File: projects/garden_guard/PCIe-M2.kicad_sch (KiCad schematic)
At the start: 24 parts, among them J4 Bus_M.2_Socket_M, M1 M.2 Screw, M2 M.2 Solder Nut, M3 M.2 Solder Nut, M4 M.2 Solder Nut, M5 M.2 Solder Nut, U7 ASEK-32.768KHZ-L-R-T, U8 AP3441SHE-7B

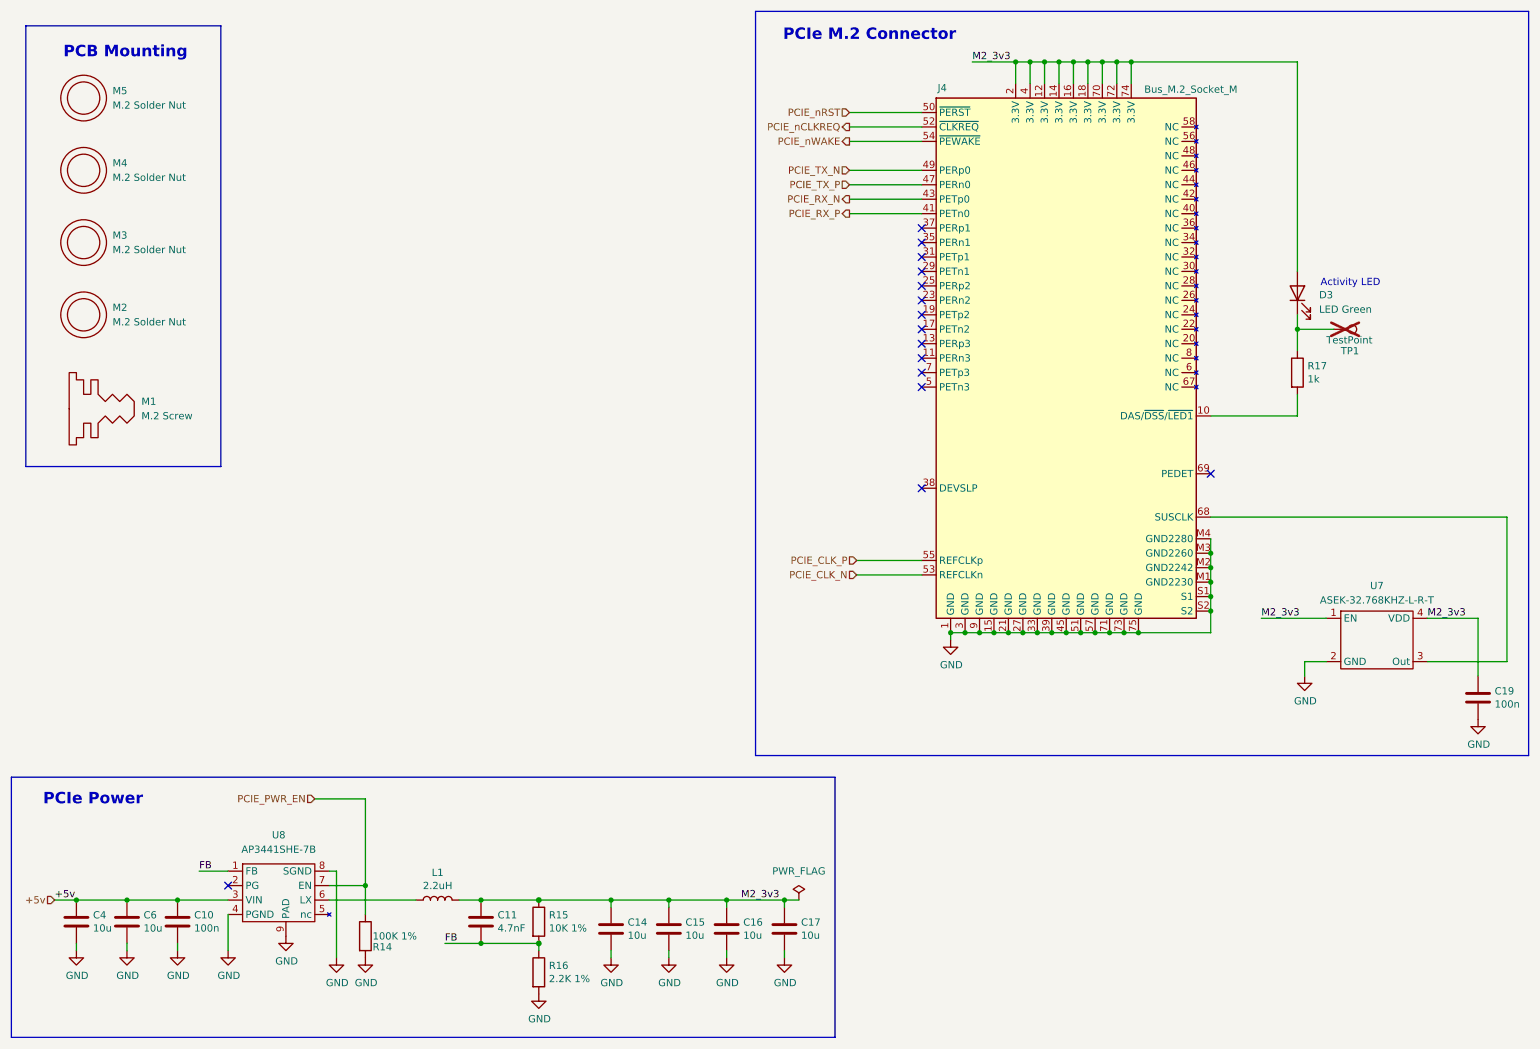
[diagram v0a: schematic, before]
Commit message: - Add PoE 12V power module - Add 12V->5V buck - Add automatic power source selection between PoE 5V and USB 5V
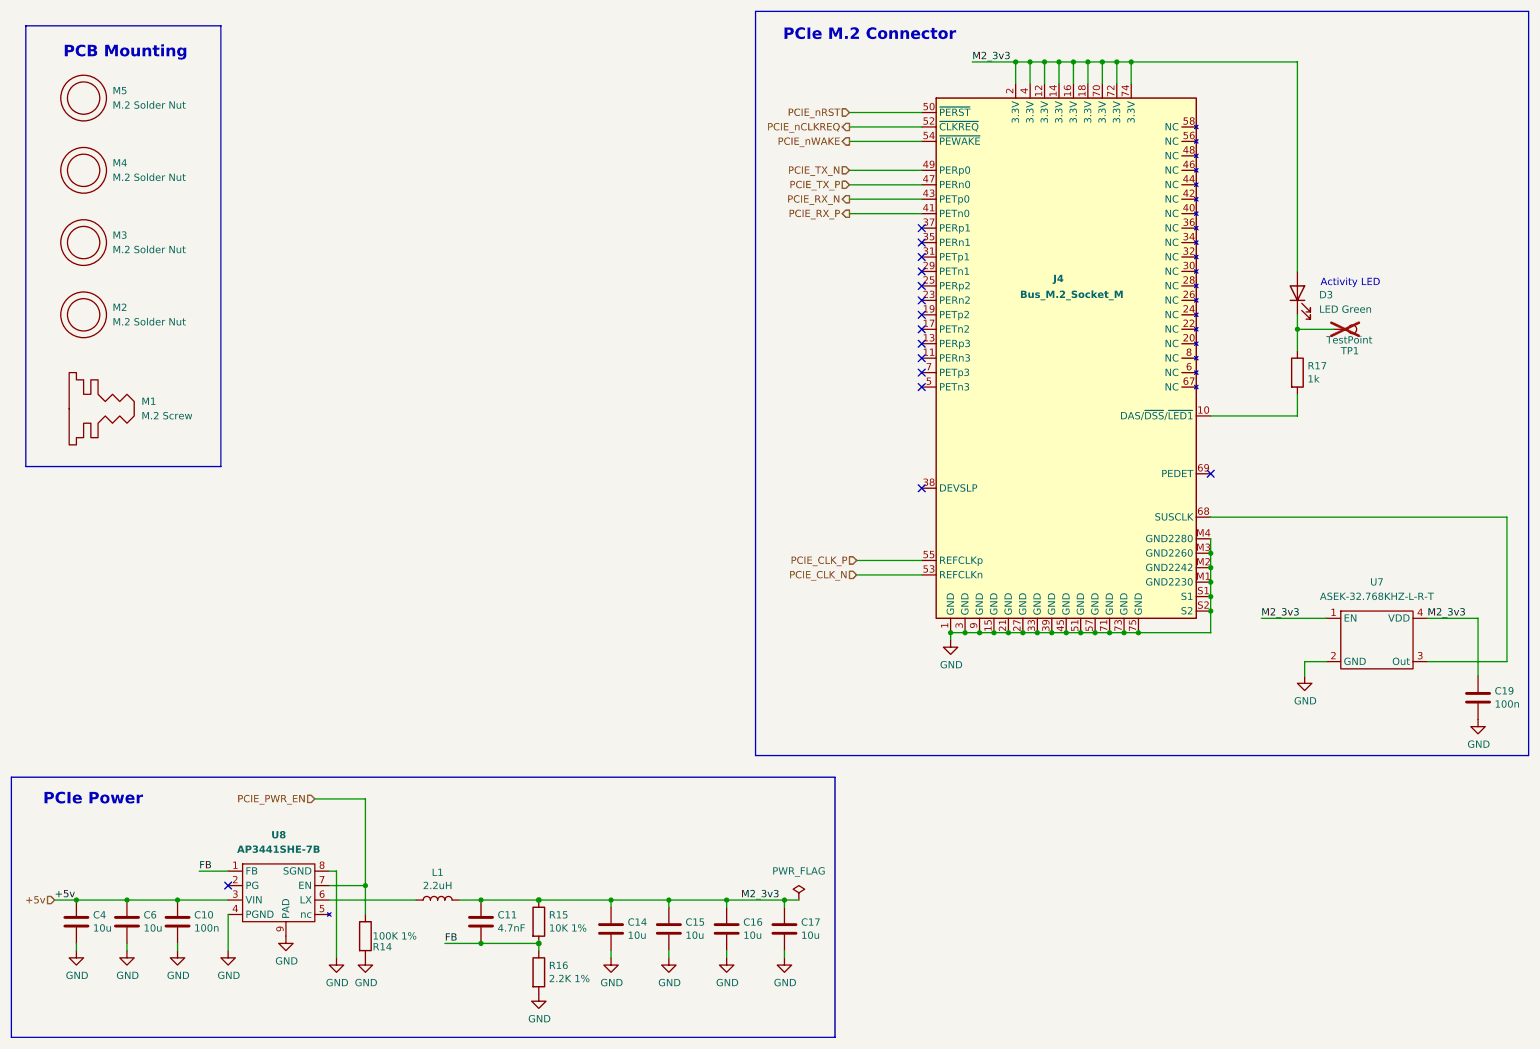
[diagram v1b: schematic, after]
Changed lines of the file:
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@@
 		(fields_autoplaced yes)
 		(property "Reference" "U7"
-			(at 254 116.205 0)
+			(at 254 115.57 0)
 			(effects
 				(font
@@
 		)
 		(property "Value" "ASEK-32.768KHZ-L-R-T"
-			(at 254 118.745 0)
+			(at 254 118.11 0)
 			(effects
 				(font
@@
 				(font
 					(size 1.27 1.27)
+					(thickness 0.254)
+					(bold yes)
 				)
 			)
@@
 				(font
 					(size 1.27 1.27)
+					(thickness 0.254)
+					(bold yes)
 				)
 			)
@@
 		(dnp no)
 		(property "Reference" "J4"
-			(at 176.784 28.702 0)
-			(effects
-				(font
-					(size 1.27 1.27)
+			(at 197.104 62.23 0)
+			(effects
+				(font
+					(size 1.27 1.27)
+					(thickness 0.254)
+					(bold yes)
 				)
 				(justify left)
@@
 		)
 		(property "Value" "Bus_M.2_Socket_M"
-			(at 213.106 28.956 0)
-			(effects
-				(font
-					(size 1.27 1.27)
-				)
-				(justify left)
+			(at 191.262 65.024 0)
+			(effects
+				(font
+					(size 1.27 1.27)
+					(thickness 0.254)
+					(bold yes)
+				)
+				(justify left)

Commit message: - Add all missing footprints - Add specific part numbers to each component in schematic
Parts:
- D3: footprint (none) -> LED_SMD:LED_0603_1608Metric; Field4 (none) -> Digikey; Field6 (none) -> SML-A12M8TT86N; Field7 (none) -> Rohm; Field8 (none) -> 650263301; MPN (none) -> LTST-S270KGKT; Mfr (none) -> Lite-On Inc.; Part Description (none) -> Green 572nm LED Indication - Discrete 2.2V 2-SMD, No Lead
- renumbered C17 to C10, C19 to C11, C4 to C3, C6 to C4, C10 to C5, C11 to C6, C14 to C7, C15 to C8, C16 to C9, J4 to J7, M5 to M1, M4 to M2, M2 to M4, M1 to M5, R14 to R12, R15 to R13, R16 to R14, R17 to R15, TP1 to TP5, U8 to U5, U7 to U6

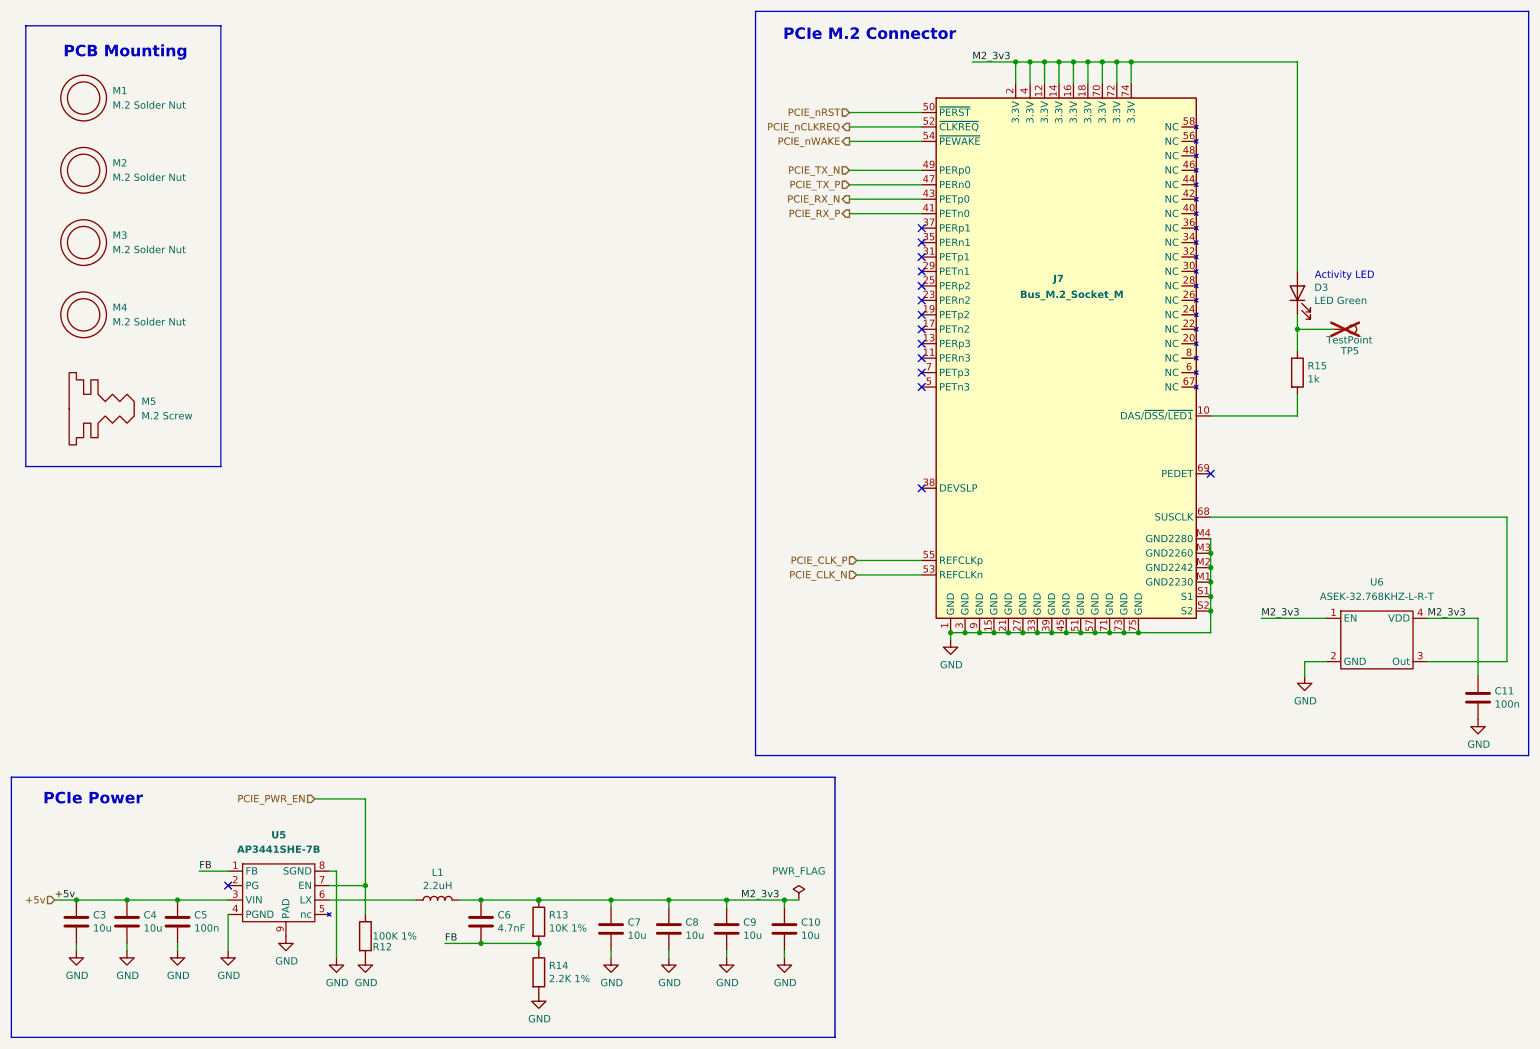
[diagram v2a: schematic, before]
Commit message: - Find part numbers for CM5 parts - Minor CM5 symbol, footprint adjustments - Move to uniform small resistor and capacitor symbols - Add *lck to .gitignore
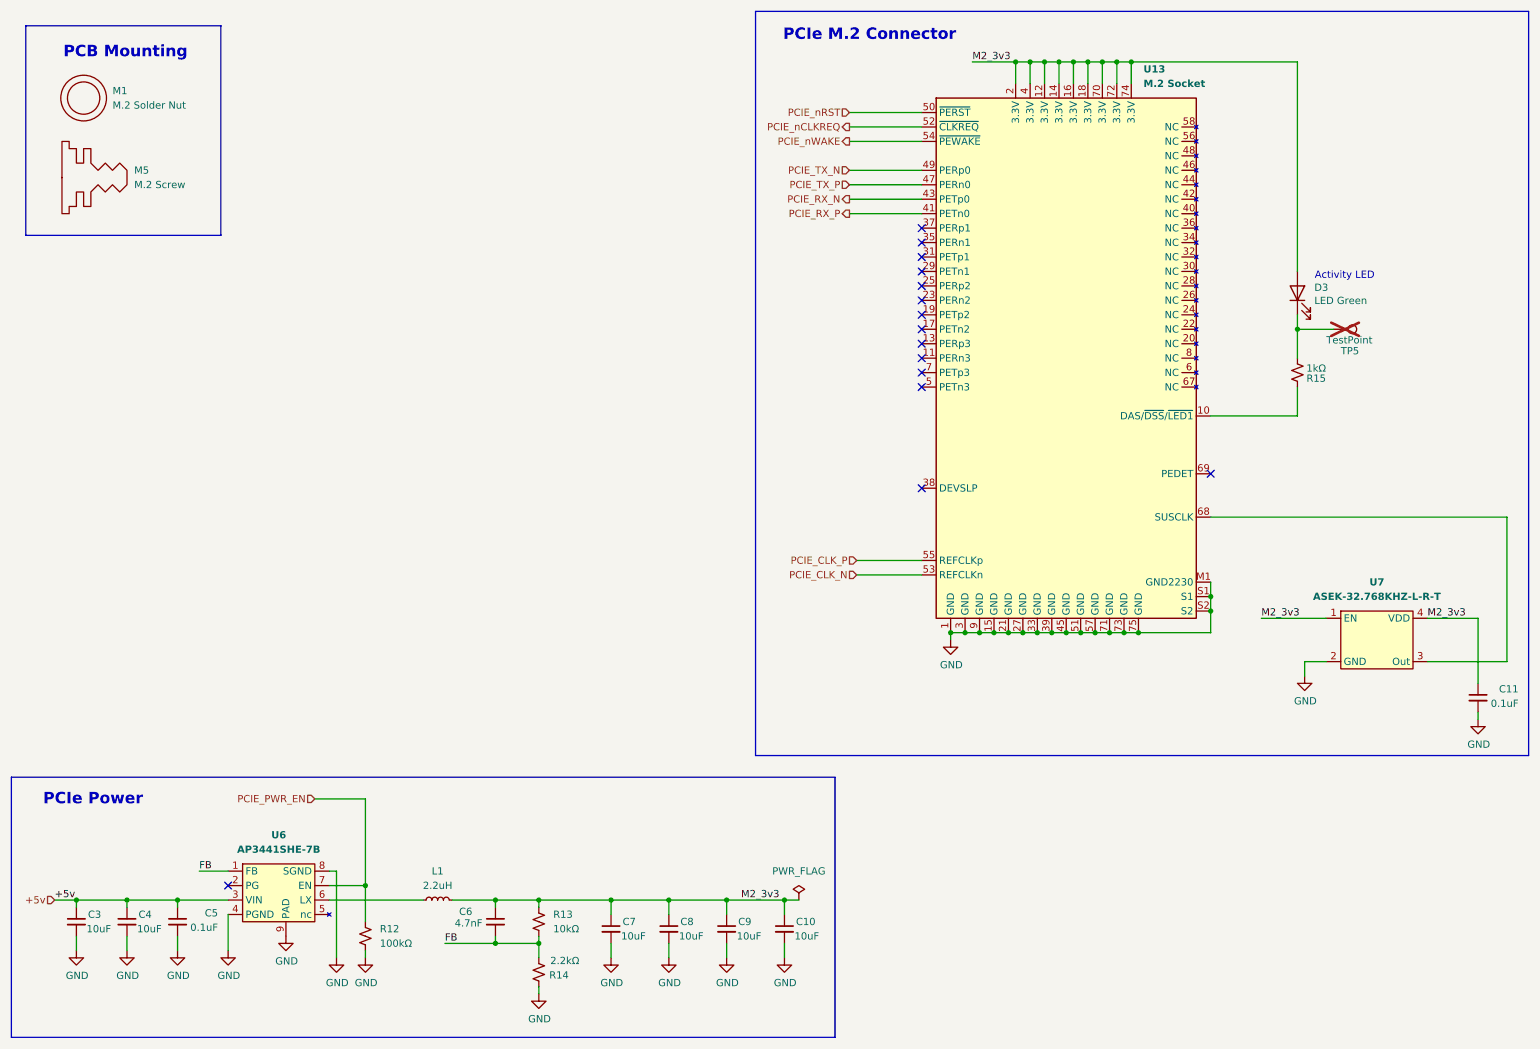
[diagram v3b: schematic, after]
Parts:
- removed C10, C3, C4, C7, C8, C9: 10u, Capacitor_SMD:C_0805_2012Metric, symbol Device:C
- removed C11, C5: 100n, Capacitor_SMD:C_0402_1005Metric, symbol Device:C
- removed C6: 4.7nF, Capacitor_SMD:C_0402_1005Metric, symbol Device:C
- removed J7: Bus_M.2_Socket_M, CM5IO:M.2 M Key socket, symbol CM5IO:Bus_M.2_Socket_M
- removed L1: 2.2uH, CM5IO:L_Bourns_SRP5030CC, symbol Device:L
- removed M2, M3, M4: M.2 Solder Nut, symbol CM5IO:SolderNut
- removed R12: 100K 1%, Resistor_SMD:R_0402_1005Metric, symbol Device:R
- removed R13: 10K 1%, Resistor_SMD:R_0402_1005Metric, symbol Device:R
- removed R14: 2.2K 1%, Resistor_SMD:R_0402_1005Metric, symbol Device:R
- removed R15: 1k, Resistor_SMD:R_0402_1005Metric, symbol Device:R
- added C10, C3, C4, C7, C8, C9: 10uF, Capacitor_SMD:C_0805_2012Metric, symbol Device:C_Small
- added C11, C5: 0.1uF, Resistor_SMD:R_0603_1608Metric, symbol Device:C_Small
- added C6: 4.7nF, Resistor_SMD:R_0603_1608Metric, symbol Device:C_Small
- added L1: 2.2uH, Capacitor_SMD:C_2220_5750Metric, symbol Device:L_Small
- added R12: 100kΩ, Resistor_SMD:R_0603_1608Metric, symbol Device:R_Small_US
- added R13: 10kΩ, Resistor_SMD:R_0603_1608Metric, symbol Device:R_Small_US
- added R14: 2.2kΩ, Resistor_SMD:R_0201_0603Metric, symbol Device:R_Small_US
- added R15: 1kΩ, Resistor_SMD:R_0603_1608Metric, symbol Device:R_Small_US
- added U13: M.2 Socket, Custom_Connector:M.2 M Key socket (2230), symbol Custom_Connector:M.2_Socket_(2230)
- U6: renamed from U5; MPN (none) -> AP3441SHE-7B; Mfr (none) -> Diodes Incorporated
- U7: renamed from U6; MPN (none) -> ASEK-32.768KHZ-L-R-T; Mfr (none) -> Abracon LLC
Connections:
- net +5v: now also C3.1, C4.1, C5.1
- net FB: now also C6.2, R13.2, R14.1
- net GND: now also C10.2, C11.2, C3.2, C4.2, C5.2, C7.2, C8.2, C9.2, R12.2, R14.2, U13.1 (GND), U13.15 (GND), U13.21 (GND), U13.27 (GND), U13.3 (GND), U13.33 (GND), U13.39 (GND), U13.45 (GND), U13.51 (GND), U13.57 (GND), U13.71 (GND), U13.73 (GND), U13.75 (GND), U13.9 (GND), U13.M1 (GND2230), U13.S1, U13.S2
- net M2_3v3: now also C10.1, C11.1, C6.1, C7.1, C8.1, C9.1, L1.2, R13.1, U13.12 (3.3V), U13.14 (3.3V), U13.16 (3.3V), U13.18 (3.3V), U13.2 (3.3V), U13.4 (3.3V), U13.70 (3.3V), U13.72 (3.3V), U13.74 (3.3V)
- net PCIE_CLK_N: now also U13.53 (REFCLKn)
- net PCIE_CLK_P: now also U13.55 (REFCLKp)
- net PCIE_PWR_EN: now also R12.1
- net PCIE_RX_N: now also U13.43 (PETp0)
- net PCIE_RX_P: now also U13.41 (PETn0)
- net PCIE_TX_N: now also U13.49 (PERp0)
- net PCIE_TX_P: now also U13.47 (PERn0)
- net PCIE_nCLKREQ: now also U13.52 (~{CLKREQ})
- net PCIE_nRST: now also U13.50 (~{PERST})
- net PCIE_nWAKE: now also U13.54 (~{PEWAKE})
- net at D3.1 (K), TP5.1: now also R15.1
- net at U6.6 (LX): now also L1.1
- net at U7.3 (Out): now also U13.68 (SUSCLK)
- new net: R15.2, U13.10 (DAS/~{DSS}/~{LED1})
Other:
- moved on the sheet: M5

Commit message: - Assign 3D models to lingering footprints lacking them - Start playing with board layout - Move CM5 library files from project to components dir
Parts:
- renumbered M5 to M2, U13 to U7, U7 to U8
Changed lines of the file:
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@@
 		(dnp no)
 		(fields_autoplaced yes)
-		(property "Reference" "U7"
+		(property "Reference" "U8"
 			(at 254 115.57 0)
 			(effects
@@
 			(project "garden_guard"
 				(path "/dcdac9d4-ef08-426f-b97c-7b9219501e71/5751e26b-0975-4f8f-84d7-7785f65d80bc"
-					(reference "U7")
+					(reference "U8")
 					(unit 1)
 				)
@@
 		(on_board no)
 		(dnp no)
-		(property "Reference" "M5"
+		(property "Reference" "M2"
 			(at 35.56 43.1799 0)
 			(effects
@@
 			(project "garden_guard"
 				(path "/dcdac9d4-ef08-426f-b97c-7b9219501e71/5751e26b-0975-4f8f-84d7-7785f65d80bc"
-					(reference "M5")
+					(reference "M2")
 					(unit 1)
 				)
@@
 		(dnp no)
 		(fields_autoplaced yes)
-		(property "Reference" "U13"
+		(property "Reference" "U7"
 			(at 212.9633 25.4 0)
 			(effects
@@
 			(project ""
 				(path "/dcdac9d4-ef08-426f-b97c-7b9219501e71/5751e26b-0975-4f8f-84d7-7785f65d80bc"
-					(reference "U13")
+					(reference "U7")
 					(unit 1)
 				)

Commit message: - Add M.2 power and connector layout - Add micro HDMI to schematic and layout - Add microSD layout - Add IR illuminator and solenoid output MOSFET layouts - Add USB-C layout
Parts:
- L1: footprint Capacitor_SMD:C_2220_5750Metric -> CM5IO:L_Bourns_SRP5030CC
- R14: footprint Resistor_SMD:R_0201_0603Metric -> Resistor_SMD:R_0603_1608Metric
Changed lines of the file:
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@@
 			)
 		)
-		(property "Footprint" "Resistor_SMD:R_0201_0603Metric"
+		(property "Footprint" "Resistor_SMD:R_0603_1608Metric"
 			(at 106.68 184.15 0)
 			(effects
@@
 			)
 		)
-		(property "Description" ""
+		(property "Description" "M.2 Socket (2230)"
 			(at 199.39 73.66 0)
 			(effects
@@
 			)
 		)
-		(property "Footprint" "Capacitor_SMD:C_2220_5750Metric"
+		(property "Footprint" "CM5IO:L_Bourns_SRP5030CC"
 			(at 88.9 171.45 0)
 			(effects
